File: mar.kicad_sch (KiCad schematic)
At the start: 17 parts, among them SW3 SW_DIP_x04, SW4 SW_SPDT, U18 74LS157, U19 74LS173

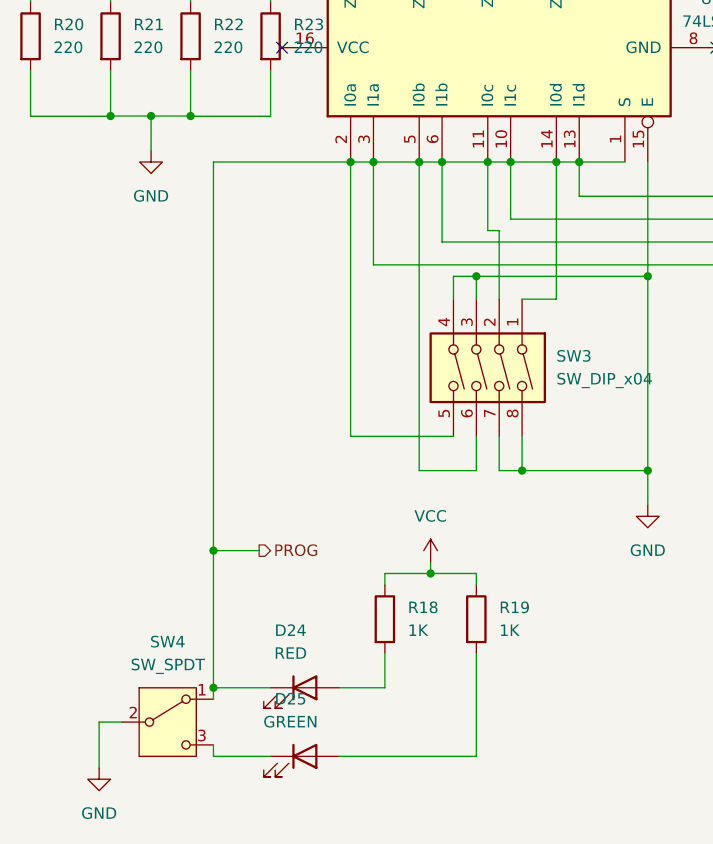
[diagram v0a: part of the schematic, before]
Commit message: Made the ram module as well as set up a custom symbol for the 74f189sj chip.
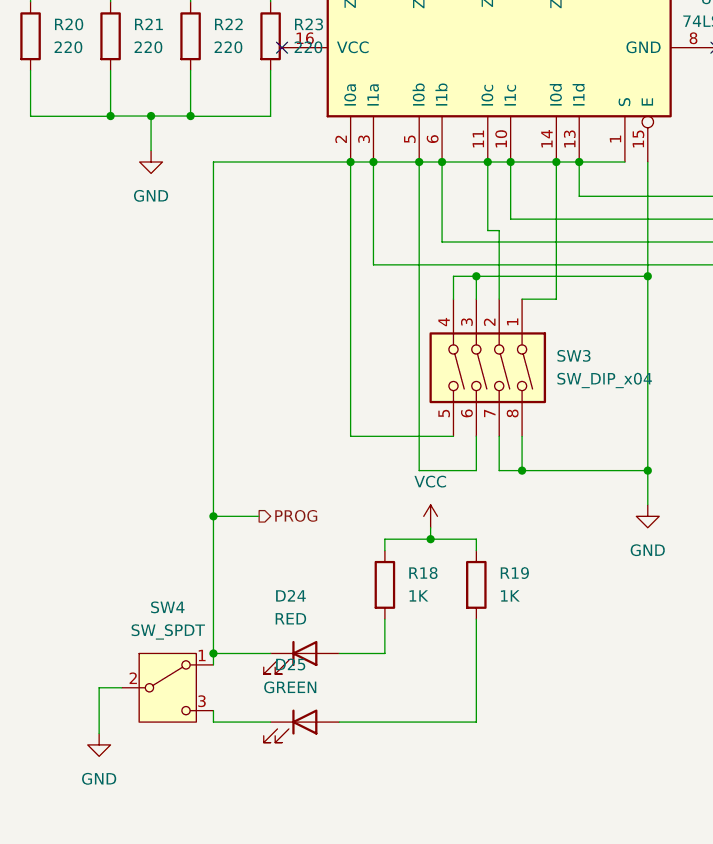
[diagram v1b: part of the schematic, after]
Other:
- moved on the sheet: D24, D25, R18, R19, SW4
